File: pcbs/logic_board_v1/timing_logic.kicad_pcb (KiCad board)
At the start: 4 copper layers, 100 x 100 mm, 103 parts, among them J1 VCC, J2 VEE, J3 NIM_COINC, J4 NIM2, J5 NIM1, J6 Input1, J7 Input2, Q1 BFR92, Q2 BFR92, Q3 BFR92, Q4 BFR92, Q5 BFR92, Q6 BFR92, U1 8240026, U2 MAX9600EUP, U3 OPA177GP, U4 REF03GS, U5 MC100EP05DG

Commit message: Add files via upload
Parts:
- C1, C10, C11, C12, C13, C14, C15, C16, C17, C18, C19, C2, C20, C21, C3, C4, C5, C6, C7, C8, C9: footprint Capacitor_SMD:C_0201_0603Metric -> Capacitor_SMD:C_0603_1608Metric_Pad1.08x0.95mm_HandSolder
- R1, R10, R11, R12, R13, R14, R15, R16, R17, R18, R19, R2, R20, R21, R22, R23, R24, R25, R26, R27, R28, R29, R3, R30, R4, R5, R6, R7, R8, R9: footprint Resistor_SMD:R_0201_0603Metric -> Resistor_SMD:R_0603_1608Metric_Pad0.98x0.95mm_HandSolder
- moved C16 1.61 mm to (94.7, 99.3)
- moved R19 0.66 mm to (98.8, 99.1)
- moved C14 0.56 mm to (92.8, 94.7)
- moved R18 0.47 mm to (96.6, 95.0)
- moved R20 0.44 mm to (98.9, 83.5)
- moved C15 0.36 mm to (95.4, 83.5)
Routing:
- net Earth: track 63.9 -> 57.5 mm, vias 74 -> 73
- net Net-(J6-Pad1): track 28.7 -> 31.1 mm, vias 0 -> 1
- net Net-(R18-Pad2): track 18.5 -> 16.9 mm
- net Net-(C15-Pad1): track 6.02 -> 4.79 mm
- net -5V: track 36.4 -> 35.7 mm

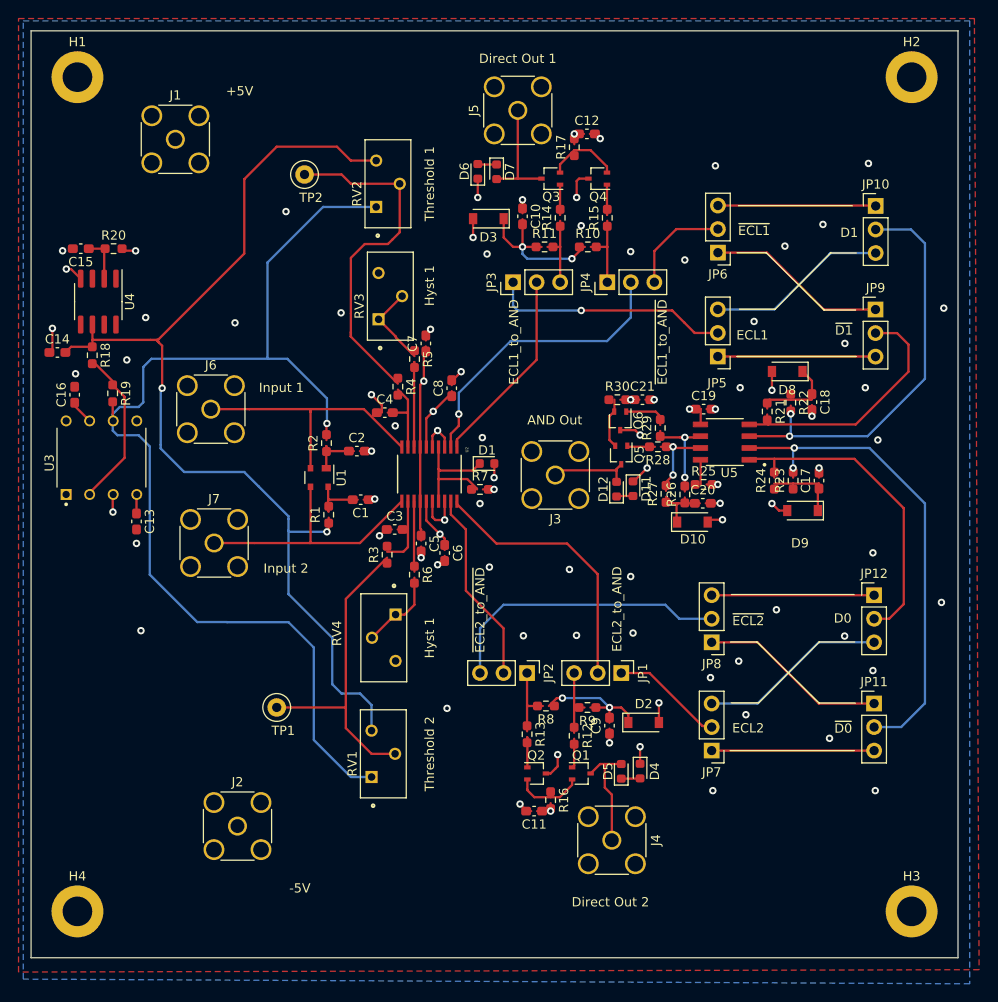
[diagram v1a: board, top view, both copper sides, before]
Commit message: changed to correct footprint sizes for resistors and caps -> fixed layout
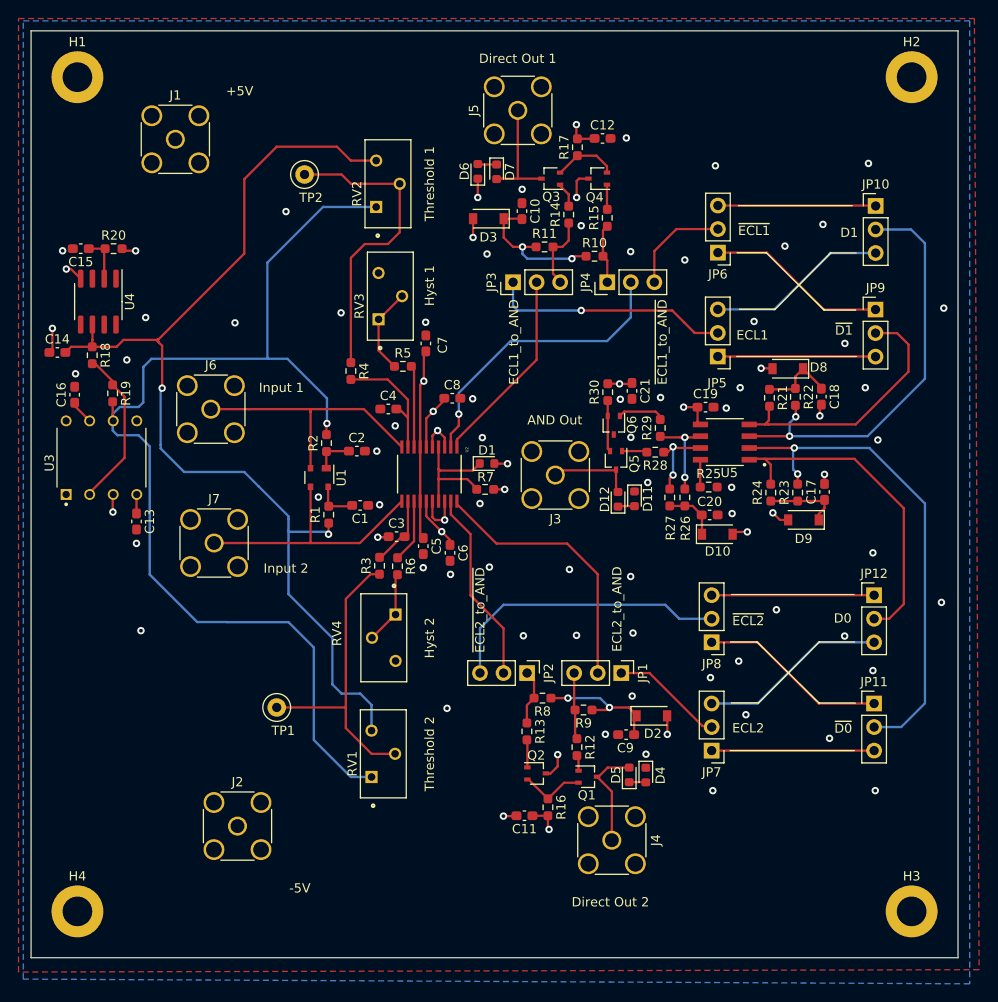
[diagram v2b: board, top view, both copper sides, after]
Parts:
- moved R4 5.34 mm to (124.5, 96.7)
- moved D10 2.98 mm to (164.0, 114.3)
- moved R6 2.04 mm to (129.5, 117.8)
- moved C9 2.04 mm to (154.2, 135.9), turned to 0 degrees
- moved C12 1.76 mm to (151.7, 71.6)
- moved R21 1.49 mm to (169.7, 99.6)
- moved R5 1.48 mm to (130.1, 96.2), turned to 0 degrees
- moved C21 1.47 mm to (154.8, 98.8), turned to -90 degrees
- moved C20 1.46 mm to (163.2, 112.2)
- moved R3 1.45 mm to (127.6, 117.7)
- moved R23 1.38 mm to (172.7, 109.8)
- moved C17 1.36 mm to (175.6, 109.7)
- moved R24 1.35 mm to (169.8, 109.8)
- moved R30 1.32 mm to (152.2, 99.0), turned to 90 degrees
- moved R12 1.26 mm to (148.9, 137.3)
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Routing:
- net Earth: track 57.5 -> 32.9 mm, vias 73 -> 76
- net Net-(C4-Pad2): track 8.85 -> 13.8 mm
- net Net-(R4-Pad1): track 38.5 -> 33.6 mm
- net Net-(J6-Pad1): track 31.1 -> 28.7 mm, vias 1 -> 0
- net Net-(JP2-Pad1): track 8.03 -> 6.01 mm
- net Net-(JP4-Pad1): track 8.41 -> 6.42 mm
- net Net-(C10-Pad2): track 17.7 -> 15.9 mm
- net Net-(R3-Pad1): track 34.2 -> 32.6 mm
- net Net-(Q1-Pad1): track 3.19 -> 1.70 mm
- net Net-(C1-Pad2): track 5.96 -> 4.69 mm
- net -5V: track 35.7 -> 36.8 mm
- net Net-(C2-Pad1): track 5.39 -> 4.34 mm
- net Net-(R6-Pad2): track 8.97 -> 7.97 mm
- net Net-(Q3-Pad2): track 7.97 -> 6.98 mm
- net ~{ECL2_to_AND_Gate}: track 35.2 -> 36.1 mm
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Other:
- board text added: "Hyst 2"
